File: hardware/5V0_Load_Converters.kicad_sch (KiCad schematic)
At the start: 78 parts, among them J19 61300311121, Q26 EPC2016C, Q27 EPC2016C, Q8 SI2302DDS-T1-GE3, U21 INA199C3DCKR, U30 LTC3833EUDC-TRPBF

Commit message: hardware: Making improvements for first release
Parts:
- C10, C11, C20, C21, C3: MPN (none) -> C0603C104K5RACTU; Manufacturer (none) -> KEMET; Package (none) -> SMD 0603; automotive Yes -> (none); automotive grade Grade 1 -> (none); capacitance 0.10 μF -> (none); category Cap -> (none); device class L1 Passive Components -> (none); device class L2 Capacitors -> (none); device class L3 Ceramic Capacitors -> (none); digikey description CAP CER 0.1UF 50V X7R 0603 -> (none); digikey part number 399-5089-2-ND -> (none); height 0.87mm -> (none); lead free Yes -> (none); library id 73022d3323b2b2b8 -> (none); manufacturer KEMET -> (none); material Ceramic -> (none); mouser part number 80-C0603C104K5R7867 -> (none); package 0603 -> (none); rohs Yes -> (none); temperature characteristic X7R -> (none); temperature coefficient 30ppm/°C -> (none); temperature range high +125°C -> (none); temperature range low -55°C -> (none); tolerance 0.1 -> (none); voltage rating 50 V -> (none)
- C12, C13: MPN (none) -> C0603C332J5GACAUTO; Manufacturer (none) -> KEMET; Package (none) -> SMD 0603; automotive Yes -> (none); automotive grade Grade 1 -> (none); capacitance 3,300 pF -> (none); category Cap -> (none); device class L1 Passive Components -> (none); device class L2 Capacitors -> (none); device class L3 Ceramic Capacitors -> (none); digikey description CAP CER 3300PF 50V C0G/NP0 0603 -> (none); digikey part number 399-16013-2-ND -> (none); height 0.87mm -> (none); lead free Yes -> (none); library id bd73e4c017624772 -> (none); manufacturer KEMET -> (none); material Ceramic -> (none); mouser description Cap Ceramic 0.0033uF 50V C0G 5% Pad SMD 0603 125C Automotiv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 -> (none); mouser part number 80-C0603C332J5GAUTO -> (none); package 0603 -> (none); rohs Yes -> (none); temperature characteristic C0G -> (none); temperature coefficient 30ppm/°C -> (none); temperature range high +125°C -> (none); temperature range low -55°C -> (none); tolerance 0.05 -> (none); voltage rating 50 V -> (none)
- C14, C15: MPN (none) -> C0603C101J5GACAUTO; Manufacturer (none) -> KEMET; Package (none) -> SMD 0603; automotive Yes -> (none); automotive grade Grade 1 -> (none); capacitance 100 pF -> (none); category Cap -> (none); device class L1 Passive Components -> (none); device class L2 Capacitors -> (none); device class L3 Ceramic Capacitors -> (none); digikey description CAP CER 100PF 50V C0G/NP0 0603 -> (none); digikey part number 399-6842-2-ND -> (none); height 0.87mm -> (none); lead free Yes -> (none); library id 9466b08f233088f0 -> (none); manufacturer KEMET -> (none); material Ceramic -> (none); mouser description Multilayer Ceramic Capacitors MLCC - SMD/SMT 100pF 50volts 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 -> (none); mouser part number 80-C0603C101J5GAUTO -> (none); package 0603 -> (none); rohs Yes -> (none); temperature characteristic C0G -> (none); temperature coefficient 30ppm/°C -> (none); temperature range high +125°C -> (none); temperature range low -55°C -> (none); tolerance 0.05 -> (none); voltage rating 50 V -> (none)
- C16, C17, C18, C19: MPN (none) -> C0603C102F3GACTU; Manufacturer (none) -> KEMET; Package (none) -> SMD 0603; automotive Yes -> (none); automotive grade Grade 1 -> (none); capacitance 1,000 pF -> (none); category Cap -> (none); device class L1 Passive Components -> (none); device class L2 Capacitors -> (none); device class L3 Ceramic Capacitors -> (none); digikey description CAP CER 1000PF 25V 1% NP0 0603 -> (none); digikey part number C0603C102F3GACTU-ND -> (none); height 0.87mm -> (none); lead free Yes -> (none); library id 46f08c8db7ea7e1d -> (none); manufacturer KEMET -> (none); material Ceramic -> (none); mouser description Capacitor, Ceramic, 1Nf, 25Vdc, 1-% Tol, 1+% Tol, C0g-Tc Co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 -> (none); mouser part number 80-C0603C102F3G -> (none); package 0603 -> (none); rohs Yes -> (none); temperature characteristic C0G -> (none); temperature coefficient 30ppm/°C -> (none); temperature range high +125°C -> (none); temperature range low -55°C -> (none); tolerance 0.01 -> (none); voltage rating 25 V -> (none)
- C22, C23: MPN (none) -> GCM32ER71H475KA55L; Manufacturer (none) -> Murata Electronics; Package (none) -> SMD 1210; automotive Yes -> (none); automotive grade Grade 1 -> (none); capacitance 4.7uF -> (none); category Cap -> (none); device class L1 Passive Components -> (none); device class L2 Capacitors -> (none); device class L3 Ceramic Capacitors -> (none); height 2.7mm -> (none); ipc land pattern name CAPC320250X250 -> (none); lead free Yes -> (none); library id 6d88f107f3aa88d3 -> (none); manufacturer Murata -> (none); material Ceramic -> (none); package 1210 -> (none); rohs Yes -> (none); temperature characteristic X7R -> (none); temperature coefficient 15% -> (none); temperature range high +125°C -> (none); temperature range low -55°C -> (none); tolerance 10% -> (none); voltage rating 50V -> (none)
- C24, C25: MPN (none) -> T495X476K035ATE300; Manufacturer (none) -> KEMET; Package (none) -> SMD 2917; automotive No -> (none); capacitance 47uF -> (none); category Cap -> (none); device class L1 Passive Components -> (none); device class L2 Capacitors -> (none); device class L3 Tantalum Capacitors -> (none); digikey description CAP TANT 47UF 10% 35V 2917 -> (none); digikey part number 399-3905-1-ND -> (none); dissipation factor 8% -> (none); esr 300mΩ -> (none); height 4.3mm -> (none); lead free Yes -> (none); leakage current 16.5uA -> (none); library id 9f2f9997282f5b7d -> (none); life 2000Hours -> (none); manufacturer Kemet -> (none); material Tantalum -> (none); mouser description Tantalum Capacitors - Solid SMD 35volts 47uF 10% ESR=300mOh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 -> (none); mouser part number 80-T495X476K35ATE300 -> (none); package 2917 -> (none); ripple current 742mA -> (none); rohs Yes -> (none); standoff height 0mm -> (none); temperature range high +125°C -> (none); temperature range low -55°C -> (none); tolerance 10% -> (none); voltage rating 35V -> (none)
- C26, C27, C28, C29: MPN (none) -> C1210C106K5RACTU; Manufacturer (none) -> KEMET; Package (none) -> SMD 1210; automotive No -> (none); capacitance 10uF -> (none); category Cap -> (none); device class L1 Passive Components -> (none); device class L2 Capacitors -> (none); device class L3 Ceramic Capacitors -> (none); digikey description CAP CER 10UF 50V X7R 1210 -> (none); digikey part number 399-11629-1-ND -> (none); height 2.8mm -> (none); ipc land pattern name CAPC320250X250 -> (none); lead free Yes -> (none); library id 80b9cd679ce51e4b -> (none); manufacturer KEMET -> (none); material Ceramic -> (none); mouser description Multilayer Ceramic Capacitors MLCC - SMD/SMT 50volts 10uF 1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 -> (none); mouser part number 80-C1210C106K5R -> (none); package 1210 -> (none); rohs Yes -> (none); temperature characteristic X7R -> (none); temperature coefficient 15% -> (none); temperature range high +125°C -> (none); temperature range low -55°C -> (none); tolerance 10% -> (none); voltage rating 50V -> (none)
- C30, C31: MPN (none) -> C0805C105K5RACTU; Manufacturer (none) -> KEMET; Package (none) -> SMD 0805; capacitance 1uF -> (none); category Cap -> (none); device class L1 Passive Components -> (none); device class L2 Capacitors -> (none); device class L3 Ceramic Capacitors -> (none); digikey description CAP CER 1UF 50V X7R 0805 -> (none); digikey part number 399-7409-2-ND -> (none); height 1.4mm -> (none); ipc land pattern name CAPC200125X787 -> (none); lead free yes -> (none); library id ac83af3950e2a3c3 -> (none); manufacturer Kemet -> (none); material Ceramic -> (none); mouser description Multilayer Ceramic Capacitors MLCC - SMD/SMT 1uF 50 Volts 1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 -> (none); mouser part number 80-C0805C105K5R -> (none); package 0805 (2012 metric) -> (none); rohs yes -> (none); standoff height 0mm -> (none); temperature characteristic X7R -> (none); temperature range high +125°C -> (none); temperature range low -55°C -> (none); tolerance 10% -> (none); voltage rating 50V -> (none)
- C32, C33: MPN (none) -> C0603C220K5RACAUTO; Manufacturer (none) -> KEMET; Package (none) -> SMD 0603; automotive Yes -> (none); automotive grade Grade 1 -> (none); capacitance 22 pF -> (none); category Cap -> (none); device class L1 Passive Components -> (none); device class L2 Capacitors -> (none); device class L3 Ceramic Capacitors -> (none); digikey description Cap Ceramic 22pF 50V X7R 10% SMD 0603 125°C Punched Paper T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 -> (none); digikey part number 399-13715-2-ND -> (none); height 0.87mm -> (none); lead free Yes -> (none); library id f369d16140aeee74 -> (none); manufacturer KEMET -> (none); material Ceramic -> (none); mouser description Cap Ceramic 22pF 50V X7R 10% SMD 0603 125°C Punched Paper T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 -> (none); mouser part number 80-C0603C220K5RAUTO -> (none); package 0603 -> (none); rohs Yes -> (none); temperature characteristic X7R -> (none); temperature coefficient 30ppm/°C -> (none); temperature range high +125°C -> (none); temperature range low -55°C -> (none); tolerance 0.1 -> (none); voltage rating 50 V -> (none)
- C34, C35, C36, C37, C38, C39: MPN (none) -> GCM32ER71C226KE19L; Manufacturer (none) -> Murata; Package (none) -> SMD 1210; automotive Yes -> (none); automotive grade Grade 1 -> (none); capacitance 22uF -> (none); category Cap -> (none); device class L1 Passive Components -> (none); device class L2 Capacitors -> (none); device class L3 Ceramic Capacitors -> (none); digikey description Cap Ceramic 22pF 50V X7R 10% SMD 0603 125°C Punched Paper T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 -> (none); digikey part number 399-13715-2-ND -> (none); height 2.7mm -> (none); ipc land pattern name CAPC320250X250 -> (none); lead free Yes -> (none); library id c3f1d06b93fd8ef7 -> (none); manufacturer Murata -> (none); material Ceramic -> (none); mouser description Cap Ceramic 22pF 50V X7R 10% SMD 0603 125°C Punched Paper T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 -> (none); mouser part number 80-C0603C220K5RAUTO -> (none); package 1210 -> (none); rohs Yes -> (none); temperature characteristic X7R -> (none); temperature coefficient 15% -> (none); temperature range high +125°C -> (none); temperature range low -55°C -> (none); tolerance 10% -> (none); voltage rating 16V -> (none)
- JP1, JP2: value SolderJumper_2_Bridged -> N/A; MPN (none) -> N/A; Manufacturer (none) -> N/A; Package (none) -> N/A
- L1, L2: MPN (none) -> 744325240; Manufacturer (none) -> Wurth Elektronik; Manufacturer_Name Wurth Elektronik -> (none); Manufacturer_Part_Number 744325240 -> (none); Mouser Part Number 710-744325240 -> (none); Mouser Price/Stock https://www.mouser.co.uk/ProductDetail/Wurth-Elektronik/744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 -> (none); Package (none) -> Non-standard
- Q26, Q27: MPN (none) -> EPC2016C; Manufacturer (none) -> EPC; Package (none) -> Die (specific to EPC2016C); automotive No -> (none); category Trans -> (none); continuous drain current 18A -> (none); depletion mode False -> (none); device class L1 Discrete Semiconductors -> (none); device class L2 Transistors -> (none); device class L3 MOSFETs -> (none); digikey description GANFET TRANS 100V 18A BUMPED DIE -> (none); digikey part number 917-1080-1-ND -> (none); drain to source breakdown voltage 100V -> (none); drain to source resistance 12mΩ -> (none); drain to source voltage 100V -> (none); gate to source voltage +6/-4V -> (none); height 0.815mm -> (none); input capacitace at vds 360pF @ 50V -> (none); lead free Yes -> (none); library id edc307fffab956cd -> (none); manufacturer EPC -> (none); max junction temp +150°C -> (none); number of N channels 1 -> (none); number of channels 1 -> (none); package SMT_2MM106_1MM632 -> (none); pulse drain current 75A -> (none); reverse recovery charge 0nC -> (none); rohs Yes -> (none); rthja max 69°C/W -> (none); standoff height 0.08mm -> (none); technology GaN -> (none); temperature range high +150°C -> (none); temperature range low -40°C -> (none); threshold vgs max 2.5V -> (none); threshold vgs min 0.8V -> (none); typ forward diode voltage 1.8V -> (none)
- Q8: Height 1.12 -> (none); MPN (none) -> SI2302DDS-T1-GE3; Manufacturer (none) -> Vishay; Manufacturer_Name Vishay -> (none); Manufacturer_Part_Number SI2302DDS-T1-GE3 -> (none); Mouser Part Number 78-SI2302DDS-T1-GE3 -> (none); Mouser Price/Stock https://www.mouser.co.uk/ProductDetail/Vishay-Semiconductor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 -> (none); Package (none) -> SOT-23-3
- R33, R34, R39, R40: Arrow Part Number CRCW0603100KFKEAHP -> (none); Arrow Price/Stock https://www.arrow.com/en/products/crcw0603100kfkeahp/vishay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 -> (none); Height 0.55 -> (none); MPN (none) -> CRCW0603100KFKEAHP; Manufacturer (none) -> Vishay; Manufacturer_Name Vishay -> (none); Manufacturer_Part_Number CRCW0603100KFKEAHP -> (none); Mouser Part Number 71-CRCW0603100KFKEAH -> (none); Mouser Price/Stock https://www.mouser.co.uk/ProductDetail/Vishay-Dale/CRCW0603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 -> (none); Package (none) -> SMD 0603
- R35, R36: MPN (none) -> CRCW060382K0FKEA; Manufacturer (none) -> Vishay; Package (none) -> SMD 0603
- R37, R38: MPN (none) -> CRCW060312K0FKEAHP; Manufacturer (none) -> Vishay; Package (none) -> SMD 0603; automotive Yes -> (none); automotive grade Grade 0 -> (none); category Res -> (none); composition Thick Film -> (none); device class L1 Passive Components -> (none); device class L2 Resistors -> (none); device class L3 Chip SMD Resistors -> (none); height 0.55mm -> (none); ipc land pattern name RESC16085X45 -> (none); lead free Yes -> (none); library id e050c09dfdbc8558 -> (none); manufacturer Vishay -> (none); package 0603 -> (none); power 250mW -> (none); power rating 0.33W -> (none); resistance 12kΩ -> (none); rohs Yes -> (none); series CRCW-HP e3 -> (none); temperature coefficient 100ppm/°C -> (none); temperature range high +155°C -> (none); temperature range low -55°C -> (none); tolerance 1% -> (none); voltage rating 75V -> (none)
- R47, R48: MPN (none) -> WSL20108L000FEA18; Manufacturer (none) -> Vishay; Package (none) -> SMD 2010
- R52, R56: MPN (none) -> CRCW060320K0FKEAHP; Manufacturer (none) -> Vishay; Package (none) -> SMD 0603; automotive Yes -> (none); automotive grade Grade 0 -> (none); category Res -> (none); composition Thick Film -> (none); device class L1 Passive Components -> (none); device class L2 Resistors -> (none); device class L3 Chip SMD Resistors -> (none); height 0.55mm -> (none); ipc land pattern name RESC16085X45 -> (none); lead free Yes -> (none); library id 6d0e00b833a89e4b -> (none); manufacturer Vishay -> (none); package 0603 -> (none); power 250mW -> (none); power rating 0.33W -> (none); resistance 20kΩ -> (none); rohs Yes -> (none); series CRCW-HP e3 -> (none); temperature coefficient 100ppm/°C -> (none); temperature range high +155°C -> (none); temperature range low -55°C -> (none); tolerance 1% -> (none); voltage rating 75V -> (none)
- R76: MPN (none) -> CRCW06030000Z0EAHP; Manufacturer (none) -> Vishay; Package (none) -> SMD 0603
- R97: MPN (none) -> CRCW0603150KFKEAHP; Manufacturer (none) -> Vishay; Package (none) -> SMD 0603
- TP2: value 5V0 -> Test point; MPN (none) -> N/A; Manufacturer (none) -> N/A; Package (none) -> N/A
- U21: footprint Package_TO_SOT_SMD:SOT-363_SC-70-6 -> footprints:INA199C3DCKR; symbol INA199C3DCKR:INA199xxDCK -> INA199C3DCKR:INA199C3DCKR; MPN (none) -> INA199C3DCKR; Manufacturer (none) -> TI; Package (none) -> SC70-6
- U30: value LTC3833EUDC-TRPBF -> LTC3833EUDC#TRPBF; symbol LTC3833EUDC#TRPBF:LTC3833EUDC-TRPBF -> LTC3833EUDC#TRPBF:LTC3833EUDC#TRPBF; MPN (none) -> LTC3833EUDC#TRPBF; Manufacturer (none) -> Analog Devices; Package (none) -> QFN-20
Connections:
- net AMUX6: no longer U21.6 (OUT)
- net GNDPWR: no longer U21.1 (REF)
- net VBUS_BK5V0: no longer U21.5 (IN-)
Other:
- moved on the sheet: C30, C31, U21

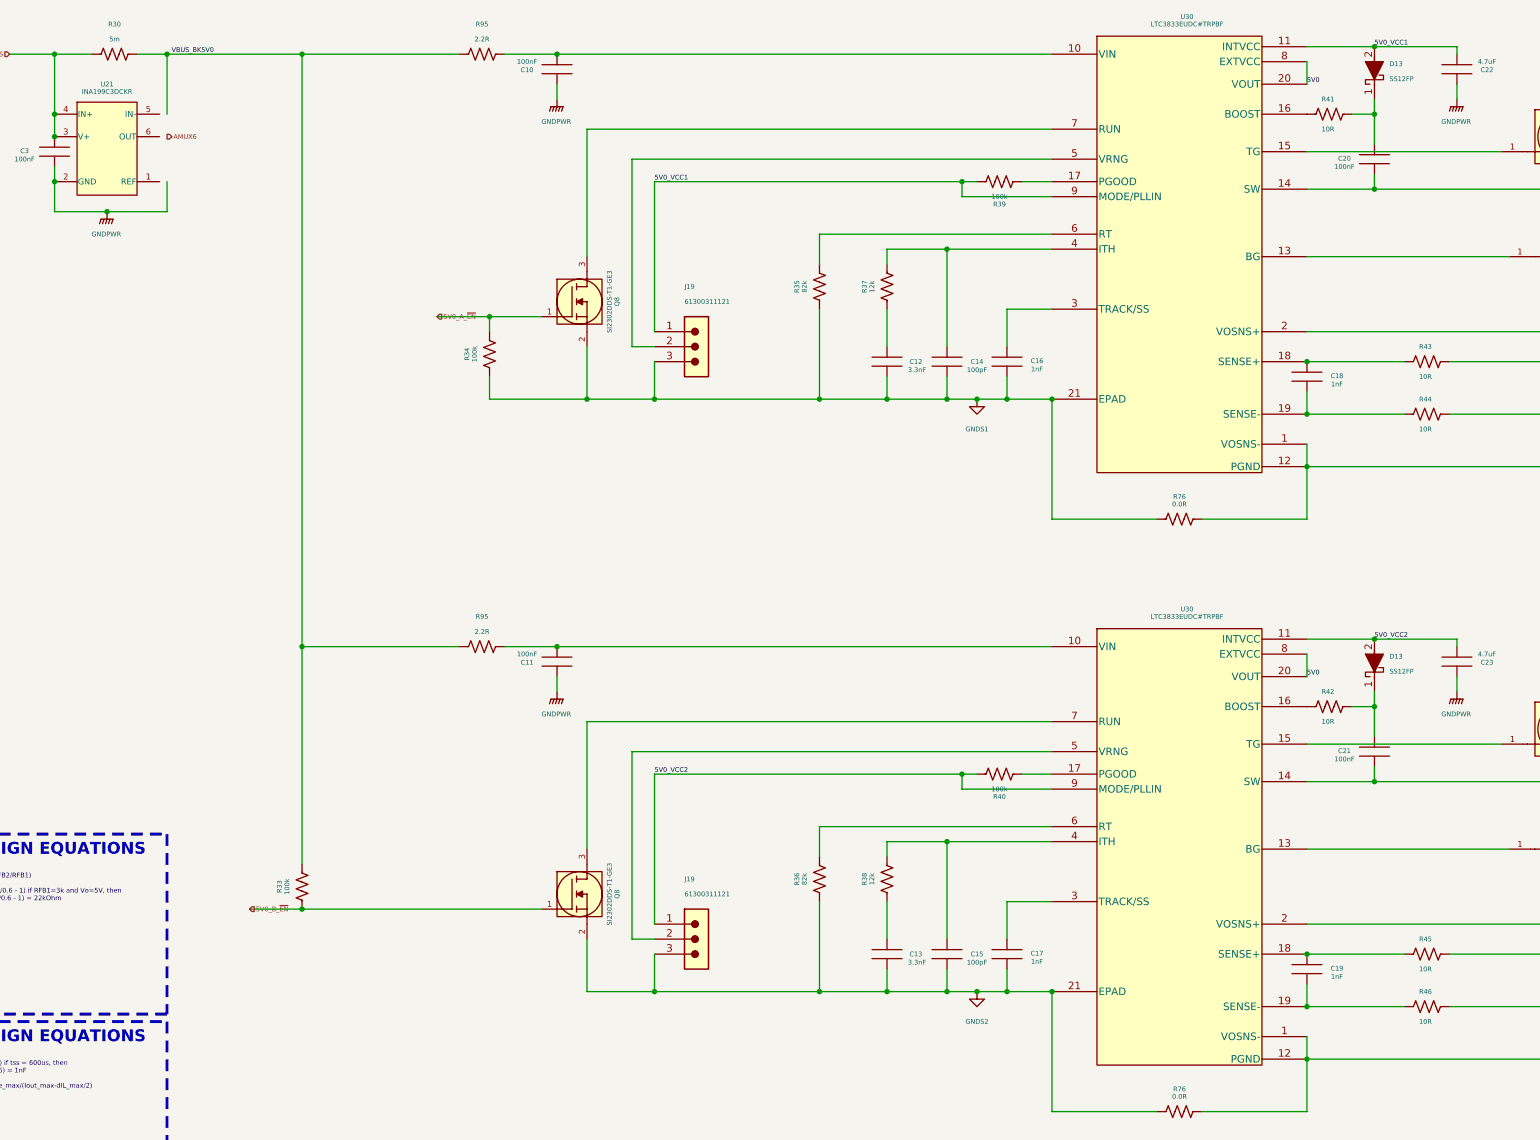
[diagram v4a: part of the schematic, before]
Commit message: hardware: Minor improvements to the schematics
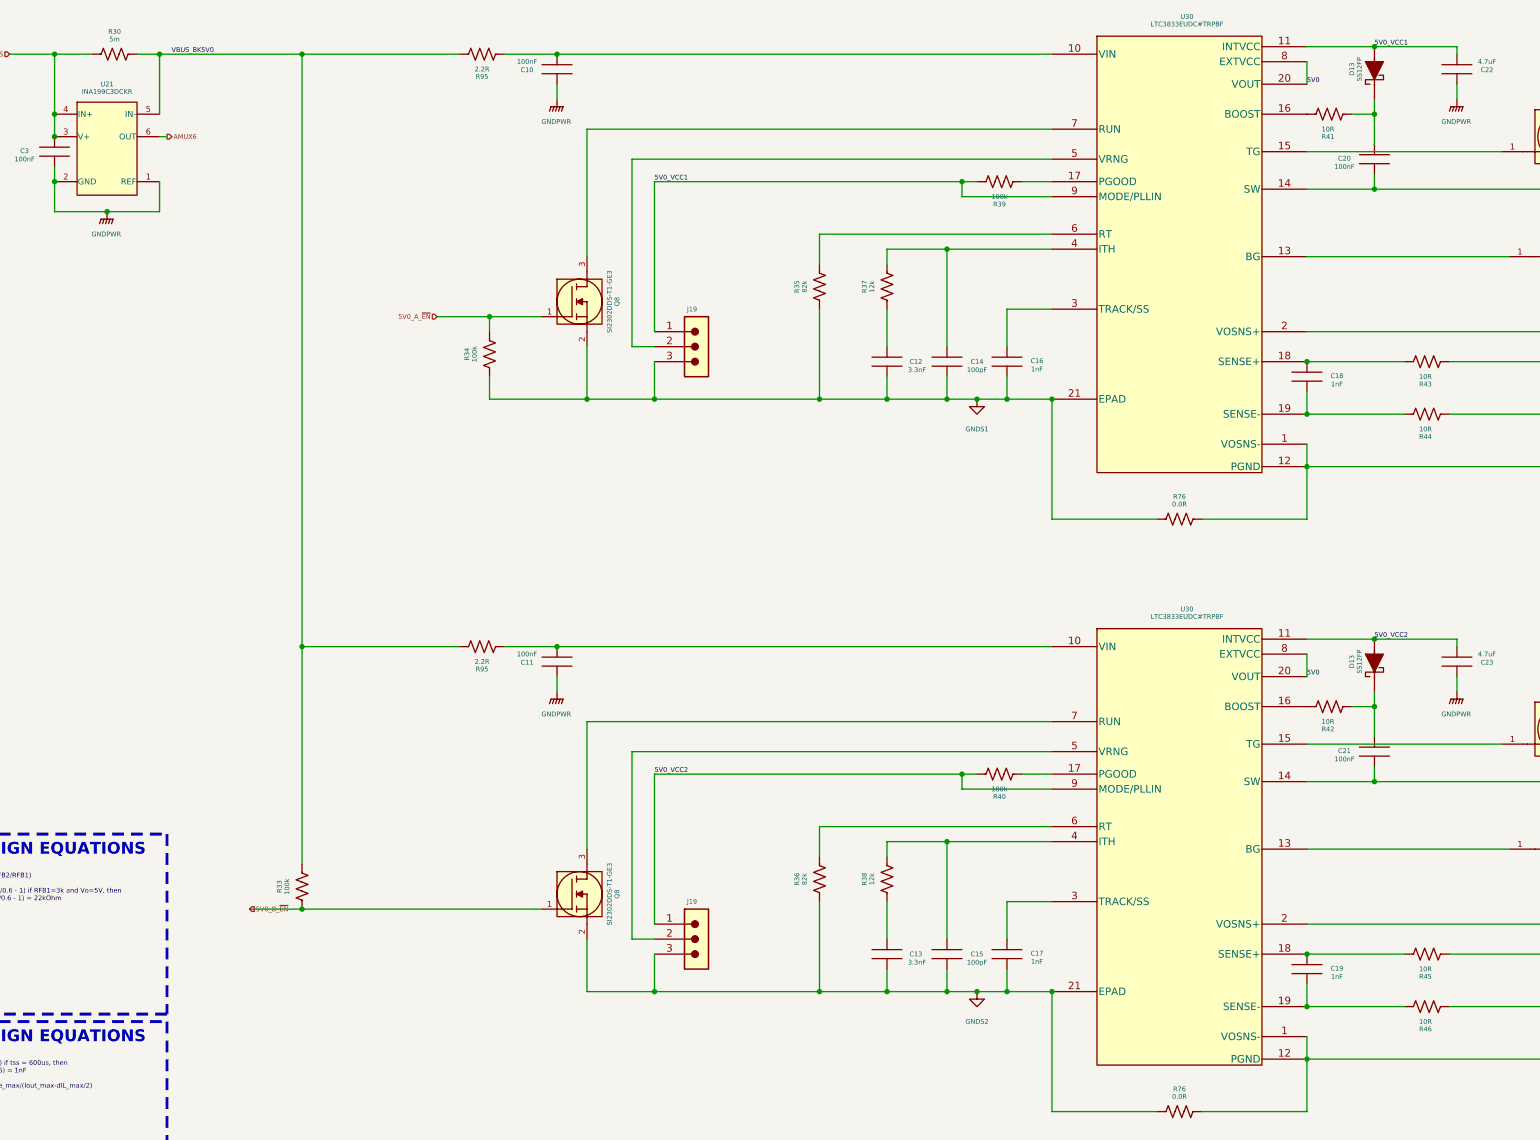
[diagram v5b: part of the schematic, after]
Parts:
- D13: Height 1 -> (none); MPN (none) -> SS12FP; Manufacturer (none) -> onsemi; Manufacturer_Name onsemi -> (none); Manufacturer_Part_Number SS12FP -> (none); Mouser Part Number 512-SS12FP -> (none); Mouser Price/Stock https://www.mouser.co.uk/ProductDetail/ON-Semiconductor-Fai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 -> (none); Package (none) -> SOD-123HE-2
- J19: value 61300311121 -> N/A; symbol 61300311121:61300311121 -> 61300311121:JUMPER_SMD; Height 8.69 -> (none); MPN (none) -> N/A; Manufacturer (none) -> N/A; Manufacturer_Name Wurth Elektronik -> (none); Manufacturer_Part_Number 61300311121 -> (none); Mouser Part Number 710-61300311121 -> (none); Mouser Price/Stock https://www.mouser.co.uk/ProductDetail/Wurth-Elektronik/613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 -> (none); Package (none) -> N/A
- Q26, Q27: Package Die (specific to EPC2016C) -> Non-standard
- R30: MPN (none) -> WSL20105L000FEA; Manufacturer (none) -> Vishay; Package (none) -> SMD 2010
- R41, R42, R43, R44, R45, R46: Arrow Part Number CRCW060310R0FKEAHP -> (none); Arrow Price/Stock https://www.arrow.com/en/products/crcw060310r0fkeahp/vishay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 -> (none); Height 0.5 -> (none); MPN (none) -> CRCW060310R0FKEAHP; Manufacturer (none) -> Vishay; Manufacturer_Name Vishay -> (none); Manufacturer_Part_Number CRCW060310R0FKEAHP -> (none); Mouser Part Number 71-CRCW060310R0FKEAH -> (none); Mouser Price/Stock https://www.mouser.co.uk/ProductDetail/Vishay-Dale/CRCW0603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 -> (none); Package (none) -> SMD 0603
- R95: MPN (none) -> CRCW06032R20FKEAHP; Manufacturer (none) -> Vishay; Package (none) -> SMD 0603
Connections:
- net AMUX6: now also U21.6 (OUT)
- net GNDPWR: now also U21.1 (REF)
- net VBUS_BK5V0: now also U21.5 (IN-)

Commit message: hardware: Adding a block diagram of the RE²PS and making minor modifications to the symbols and schematic
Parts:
- J19: symbol 61300311121:JUMPER_SMD -> JUMPER_SMD:JUMPER_SMD; Observations (none) -> The resistor CRCW06030000Z0EAHP (SMD 0603) is connected bet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
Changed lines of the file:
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@@
     )
   )
-  (symbol (lib_id "61300311121:JUMPER_SMD") (at 134.62 172.72 0) (unit 1)
+  (symbol (lib_id "JUMPER_SMD:JUMPER_SMD") (at 134.62 172.72 0) (unit 1)
     (in_bom yes) (on_board yes) (dnp no)
     (property "Reference" "J19" (at 140.97 168.91 0) (do_not_autoplace)
@@
     )
     (property "Package" "N/A" (at 135.89 196.85 0)
+      (effects (font (size 1.27 1.27)) hide)
+    )
+    (property "Observations" "The resistor CRCW06030000Z0EAHP (SMD 0603) is connected between pins 1 and 2" (at 134.62 182.88 0)
       (effects (font (size 1.27 1.27)) hide)
     )
@@
     )
   )
-  (symbol (lib_id "61300311121:JUMPER_SMD") (at 134.62 72.39 0) (unit 1)
+  (symbol (lib_id "JUMPER_SMD:JUMPER_SMD") (at 134.62 72.39 0) (unit 1)
     (in_bom yes) (on_board yes) (dnp no)
     (property "Reference" "J19" (at 140.97 68.58 0) (do_not_autoplace)
@@
       (effects (font (size 1.27 1.27)) hide)
     )
+    (property "Observations" "The resistor CRCW06030000Z0EAHP (SMD 0603) is connected between pins 1 and 2" (at 134.62 82.55 0)
+      (effects (font (size 1.27 1.27)) hide)
+    )

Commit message: hardware: Minor modifications for the upcoming release
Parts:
- TP2: MPN N/A -> S2761-46R; Manufacturer N/A -> Harwin; Package N/A -> Non-standard
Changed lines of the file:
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@@
       (effects (font (size 1.27 1.27)) hide)
     )
-    (property "Datasheet" "N/A" (at 266.7 270.51 0)
+    (property "Datasheet" "https://br.mouser.com/datasheet/2/181/S2761R-1291319.pdf" (at 266.7 270.51 0)
       (effects (font (size 1.27 1.27)) hide)
     )
-    (property "MPN" "N/A" (at 269.24 270.51 0)
+    (property "MPN" "S2761-46R" (at 269.24 270.51 0)
       (effects (font (size 1.27 1.27)) hide)
     )
-    (property "Package" "N/A" (at 271.78 270.51 0)
+    (property "Package" "Non-standard" (at 271.78 270.51 0)
       (effects (font (size 1.27 1.27)) hide)
     )
-    (property "Manufacturer" "N/A" (at 274.32 270.51 0)
+    (property "Manufacturer" "Harwin" (at 274.32 270.51 0)
       (effects (font (size 1.27 1.27)) hide)
     )

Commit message: hardware: update schematic and layout projects
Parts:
- R49, R51, R53, R55, RGND1, RGND2: renamed from R76; value 0.0R -> 0R
- renumbered C3 to C9, D13 to D1, D13 to D4, J19 to J20, Q8 to Q1, Q26 to Q11, Q27 to Q12, Q8 to Q2, Q27 to Q3, Q26 to Q4, R95 to R31, R95 to R32, R97 to R50, R97 to R54, TP2 to TP4, U21 to U22, U30 to U23, U30 to U26
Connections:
- net GNDPWR: now also C24.2, C25.2; no longer C24.1 (CATHODE), C25.1 (CATHODE)
- net VBUS_BK5V0: now also C24.1, C25.1; no longer C24.2 (ANODE), C25.2 (ANODE)
